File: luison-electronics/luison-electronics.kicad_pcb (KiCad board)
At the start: 2 copper layers, 83.2 x 64.8 mm, 26 parts, among them SW3 EECO_Micro-Dip_3500_B02, U2 Robochallenge_KillSwitch

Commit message: asd
asd
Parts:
- added PS10: COOLER, luison-electronics:JST_XH_B3B-XH-A_1x03_P2.50mm_Vertical, F.Cu at (175.9, 116.8)
- moved ? 3.18 mm to (167.6, 104.8)
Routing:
- net +24V: track 184.4 -> 191.5 mm
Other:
- board text added: "+24"
- board text added: "G"
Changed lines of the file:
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@@
   (net 41 "/6")
   (net 42 "/7")
+  (net 43 "unconnected-(PS10-Signal-Pad2)")
   (footprint "luison-electronics:JST_XH_B3B-XH-A_1x03_P2.50mm_Vertical" (layer "F.Cu")
     (at 182.245 108.585)
@@
   )
   (footprint "" (layer "F.Cu")
-    (at 170.815 104.775)
+    (at 167.64 104.775)
     (fp_text reference "" (at 0 0) (layer "F.SilkS")
         (effects (font (size 1.27 1.27) (thickness 0.15)))
@@
     (pad "1" thru_hole roundrect (at 0 0 90) (size 1.524 2.54) (drill 1) (layers "*.Cu" "*.Mask") (roundrect_rratio 0.25)
       (net 1 "GND"))
+  )
+  (footprint "luison-electronics:JST_XH_B3B-XH-A_1x03_P2.50mm_Vertical" (layer "F.Cu")
+    (at 175.895 116.84 180)
+    (descr "JST XH series connector, B3B-XH-A (http://www.jst-mfg.com/product/pdf/eng/eXH.pdf), generated with kicad-footprint-generator")
+    (tags "connector JST XH vertical")
+    (property "Sheetfile" "luison-electronics.kicad_sch")
+    (property "Sheetname" "")
+    (property "ki_description" "Omron Infrared Proximity Sensor")
+    (property "ki_keywords" "Digital Infrared Sensor")
+    (attr through_hole)
+    (fp_text reference "PS10" (at 2.5 -3.55) (layer "F.SilkS")
+        (effects (font (size 1 1) (thickness 0.15)))
+    )
+    (fp_text value "COOLER" (at 2.5 4.6) (layer "F.Fab")
+        (effects (font (size 1 1) (thickness 0.15)))
+    )
+    (fp_text user "${REFERENCE}" (at 2.5 2.7) (layer "F.Fab")
+        (effects (font (size 1 1) (thickness 0.15)))
+    )
+    (fp_line (start -2.85 -2.75) (end -2.85 -1.5)
+      (stroke (width 0.12) (type solid)) (layer "F.SilkS"))
+    (fp_line (start -2.56 -2.46) (end -2.56 3.51)
+      (stroke (width 0.12) (type solid)) (layer "F.SilkS"))
+    (fp_line (start -2.56 3.51) (end 7.56 3.51)
+      (stroke (width 0.12) (type solid)) (layer "F.SilkS"))
+    (fp_line (start -2.55 -2.45) (end -2.55 -1.7)
+      (stroke (width 0.12) (type solid)) (layer "F.SilkS"))
+    (fp_line (start -2.55 -1.7) (end -0.75 -1.7)
+      (stroke (width 0.12) (type solid)) (layer "F.SilkS"))
+    (fp_line (start -2.55 -0.2) (end -1.8 -0.2)
+      (stroke (width 0.12) (type solid)) (layer "F.SilkS"))
+    (fp_line (start -1.8 -0.2) (end -1.8 2.75)
+      (stroke (width 0.12) (type solid)) (layer "F.SilkS"))
+    (fp_line (start -1.8 2.75) (end 2.5 2.75)
+      (stroke (width 0.12) (type solid)) (layer "F.SilkS"))
+    (fp_line (start -1.6 -2.75) (end -2.85 -2.75)
+      (stroke (width 0.12) (type solid)) (layer "F.SilkS"))
+    (fp_line (start -0.75 -2.45) (end -2.55 -2.45)
+      (stroke (width 0.12) (type solid)) (layer "F.SilkS"))
+    (fp_line (start -0.75 -1.7) (end -0.75 -2.45)
+      (stroke (width 0.12) (type solid)) (layer "F.SilkS"))
+    (fp_line (start 0.75 -2.45) (end 0.75 -1.7)
+      (stroke (width 0.12) (type solid)) (layer "F.SilkS"))
+    (fp_line (start 0.75 -1.7) (end 4.25 -1.7)
+      (stroke (width 0.12) (type solid)) (layer "F.SilkS"))
+    (fp_line (start 4.25 -2.45) (end 0.75 -2.45)
+      (stroke (width 0.12) (type solid)) (layer "F.SilkS"))
+    (fp_line (start 4.25 -1.7) (end 4.25 -2.45)
+      (stroke (width 0.12) (type solid)) (layer "F.SilkS"))
+    (fp_line (start 5.75 -2.45) (end 5.75 -1.7)
+      (stroke (width 0.12) (type solid)) (layer "F.SilkS"))
+    (fp_line (start 5.75 -1.7) (end 7.55 -1.7)
+      (stroke (width 0.12) (type solid)) (layer "F.SilkS"))
+    (fp_line (start 6.8 -0.2) (end 6.8 2.75)
+      (stroke (width 0.12) (type solid)) (layer "F.SilkS"))
+    (fp_line (start 6.8 2.75) (end 2.5 2.75)
+      (stroke (width 0.12) (type solid)) (layer "F.SilkS"))
+    (fp_line (start 7.55 -2.45) (end 5.75 -2.45)
+      (stroke (width 0.12) (type solid)) (layer "F.SilkS"))
+    (fp_line (start 7.55 -1.7) (end 7.55 -2.45)
+      (stroke (width 0.12) (type solid)) (layer "F.SilkS"))
+    (fp_line (start 7.55 -0.2) (end 6.8 -0.2)
+      (stroke (width 0.12) (type solid)) (layer "F.SilkS"))
+    (fp_line (start 7.56 -2.46) (end -2.56 -2.46)
+      (stroke (width 0.12) (type solid)) (layer "F.SilkS"))
+    (fp_line (start 7.56 3.51) (end 7.56 -2.46)
+      (stroke (width 0.12) (type solid)) (layer "F.SilkS"))
+    (fp_line (start -2.95 -2.85) (end -2.95 3.9)
+      (stroke (width 0.05) (type solid)) (layer "F.CrtYd"))
+    (fp_line (start -2.95 3.9) (end 7.95 3.9)
+      (stroke (width 0.05) (type solid)) (layer "F.CrtYd"))
+    (fp_line (start 7.95 -2.85) (end -2.95 -2.85)
+      (stroke (width 0.05) (type solid)) (layer "F.CrtYd"))
+    (fp_line (start 7.95 3.9) (end 7.95 -2.85)
+      (stroke (width 0.05) (type solid)) (layer "F.CrtYd"))
+    (fp_line (start -2.45 -2.35) (end -2.45 3.4)
+      (stroke (width 0.1) (type solid)) (layer "F.Fab"))
+    (fp_line (start -2.45 3.4) (end 7.45 3.4)
+      (stroke (width 0.1) (type solid)) (layer "F.Fab"))
+    (fp_line (start -0.625 -2.35) (end 0 -1.35)
+      (stroke (width 0.1) (type solid)) (layer "F.Fab"))
+    (fp_line (start 0 -1.35) (end 0.625 -2.35)
+      (stroke (width 0.1) (type solid)) (layer "F.Fab"))
+    (fp_line (start 7.45 -2.35) (end -2.45 -2.35)
+      (stroke (width 0.1) (type solid)) (layer "F.Fab"))
+    (fp_line (start 7.45 3.4) (end 7.45 -2.35)
+      (stroke (width 0.1) (type solid)) (layer "F.Fab"))
+    (pad "1" thru_hole roundrect (at 0 0 180) (size 1.7 2.54) (drill 1) (layers "*.Cu" "*.Mask") (roundrect_rratio 0.147059)
+      (net 4 "+24V") (pinfunction "VCC") (pintype "power_in"))
+    (pad "2" thru_hole oval (at 2.5 0 180) (size 1.7 2.54) (drill 1) (layers "*.Cu" "*.Mask")
+      (net 43 "unconnected-(PS10-Signal-Pad2)") (pinfunction "Signal") (pintype "output"))
+    (pad "3" thru_hole oval (at 5 0 180) (size 1.7 2.54) (drill 1) (layers "*.Cu" "*.Mask")
+      (net 1 "GND") (pinfunction "GND") (pintype "power_in"))
+    (model "${KICAD6_3DMODEL_DIR}/Connector_JST.3dshapes/JST_XH_B3B-XH-A_1x03_P2.50mm_Vertical.wrl"
+      (offset (xyz 0 0 0))
+      (scale (xyz 1 1 1))
+      (rotate (xyz 0 0 0))
+    )
   )
   (footprint "luison-electronics:ESP32-S2-DevKitC-1" (layer "F.Cu")
@@
     (effects (font (size 1.5 1.5) (thickness 0.3) bold) (justify left bottom))
   )
+  (gr_text "G" (at 165.1 119.38) (layer "F.Cu" knockout)
+    (effects (font (size 1.5 1.5) (thickness 0.3) bold) (justify left bottom))
+  )
   (gr_text "PSFR\n" (at 181.61 115.57) (layer "F.Cu" knockout)
     (effects (font (size 1.5 1.5) (thickness 0.3) bold) (justify left bottom))
@@
     (effects (font (size 1.5 1.5) (thickness 0.3) bold) (justify left bottom))
   )
-  (gr_text "PSFC" (at 170.815 115.57) (layer "F.Cu" knockout)
+  (gr_text "PSFC" (at 171.45 106.045) (layer "F.Cu" knockout)
+    (effects (font (size 1.5 1.5) (thickness 0.3) bold) (justify left bottom))
+  )
+  (gr_text "+24" (at 179.705 119.38) (layer "F.Cu" knockout)
     (effects (font (size 1.5 1.5) (thickness 0.3) bold) (justify left bottom))
   )
@@
   (segment (start 125.08 104.7515) (end 125.08 108.585) (width 1.5) (layer "B.Cu") (net 2))
   (segment (start 125.08 110.475) (end 125.08 108.585) (width 1.5) (layer "B.Cu") (net 2))
+  (segment (start 175.895 116.84) (end 175.895 109.935) (width 1.25) (layer "B.Cu") (net 4))
   (segment (start 182.245 108.585) (end 182.245 112.649) (width 1.5) (layer "B.Cu") (net 4))
   (segment (start 186.715 66.065) (end 172.745 66.065) (width 1.5) (layer "B.Cu") (net 4))
@@
   (segment (start 190.119 111.633) (end 188.595 113.157) (width 1.5) (layer "B.Cu") (net 4))
   (segment (start 183.896 88.265) (end 187.706 92.075) (width 1.5) (layer "B.Cu") (net 4))
+  (segment (start 175.895 109.935) (end 175.815 109.855) (width 1.25) (layer "B.Cu") (net 4))
   (segment (start 172.745 66.065) (end 172.72 66.04) (width 1.5) (layer "B.Cu") (net 4))
   (segment (start 115.316 93.265) (end 172.5305 93.265) (width 1.5) (layer "B.Cu") (net 8))

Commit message: asdf
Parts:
- removed ? (x4): , 
- removed the REF** at (141.6, 113.0)
- moved REF** 0.76 mm to (190.5, 63.0)
- renumbered PS10 to COOLER
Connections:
- MCU2 pad 24: /LS_FR -> unconnected-(MCU2-IO43-Pad24)
- MCU2 pad 25: /SDA -> /LS_FR
- MCU2 pad 26: /SCL -> /LS_BR
- MCU2 pad 27: unconnected-(MCU2-IO2/ADC-Pad27) -> /SDA
- MCU2 pad 28: /LS_BR -> /SCL
- MCU2 pad 31: /SW_P8 -> unconnected-(MCU2-IO39-Pad31)
- MCU2 pad 32: unconnected-(MCU2-IO38-Pad32) -> /SW_P8
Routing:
- net /PS_R: track 23.5 -> 15.8 mm
- net /SDA: track 21.2 -> 28.4 mm
- net /SCL: track 25.0 -> 31.9 mm
- net /LS_BR: track 7.69 -> 11.3 mm
- net /LS_FR: track 8.22 -> 9.27 mm
- net /SW_P8: track 5.71 -> 6.73 mm
- net GND: vias 0 -> 6
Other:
- board size 83.2 x 64.8 mm -> 94 x 71.8 mm
- board text added: "LUISON_ELECTRONIS"
- board text removed: "++G5"
- board text removed: "+24"
- board text removed: "764"
- board text removed: "G"
- board text removed: "G EM S +"
- board text removed: "LSBL"
- board text removed: "LSBR"
- board text removed: "LSFL"
- board text removed: "LSFR"
- board text removed: "LUISON"
- board text removed: "PSB"
- board text removed: "PSFC"
- board text removed: "PSFL"
- board text removed: "PSFR"
- board text removed: "PSL"
- board text removed: "PSR"

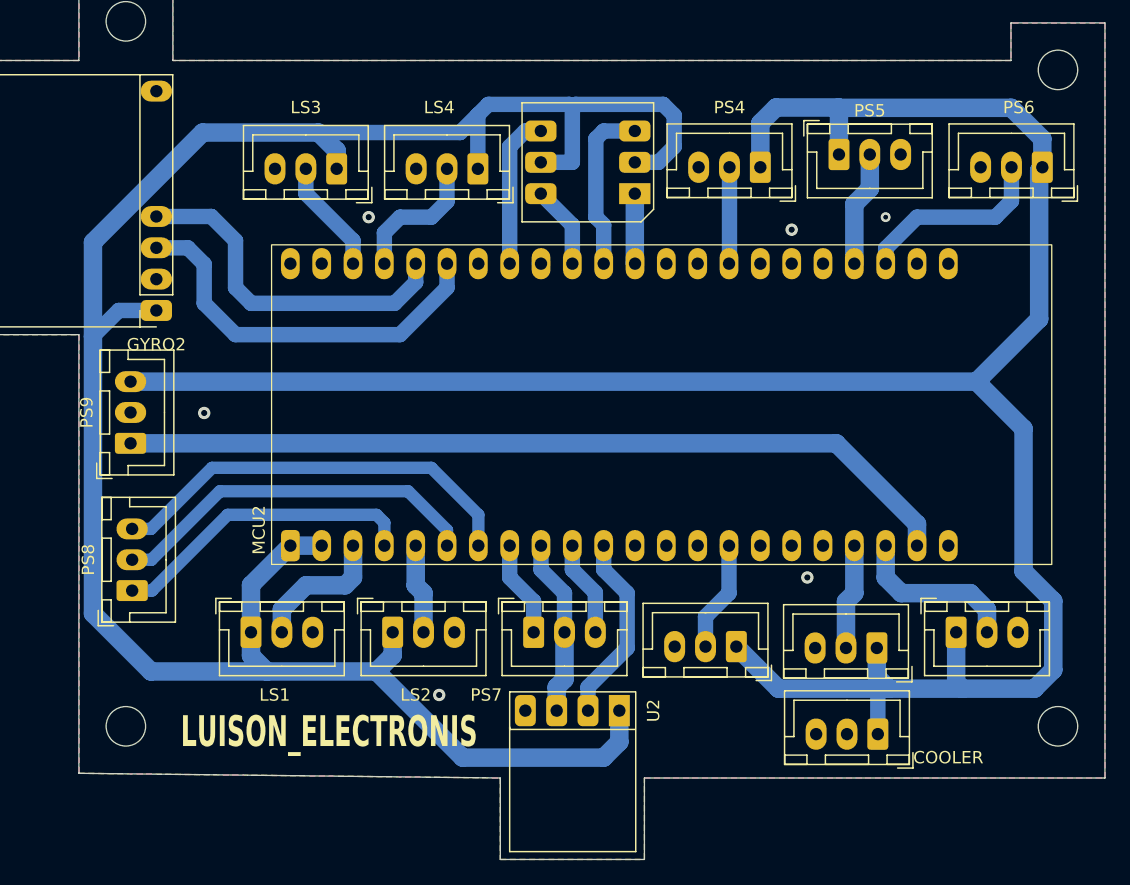
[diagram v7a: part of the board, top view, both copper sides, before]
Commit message: Update pcb with correct pins and constraints
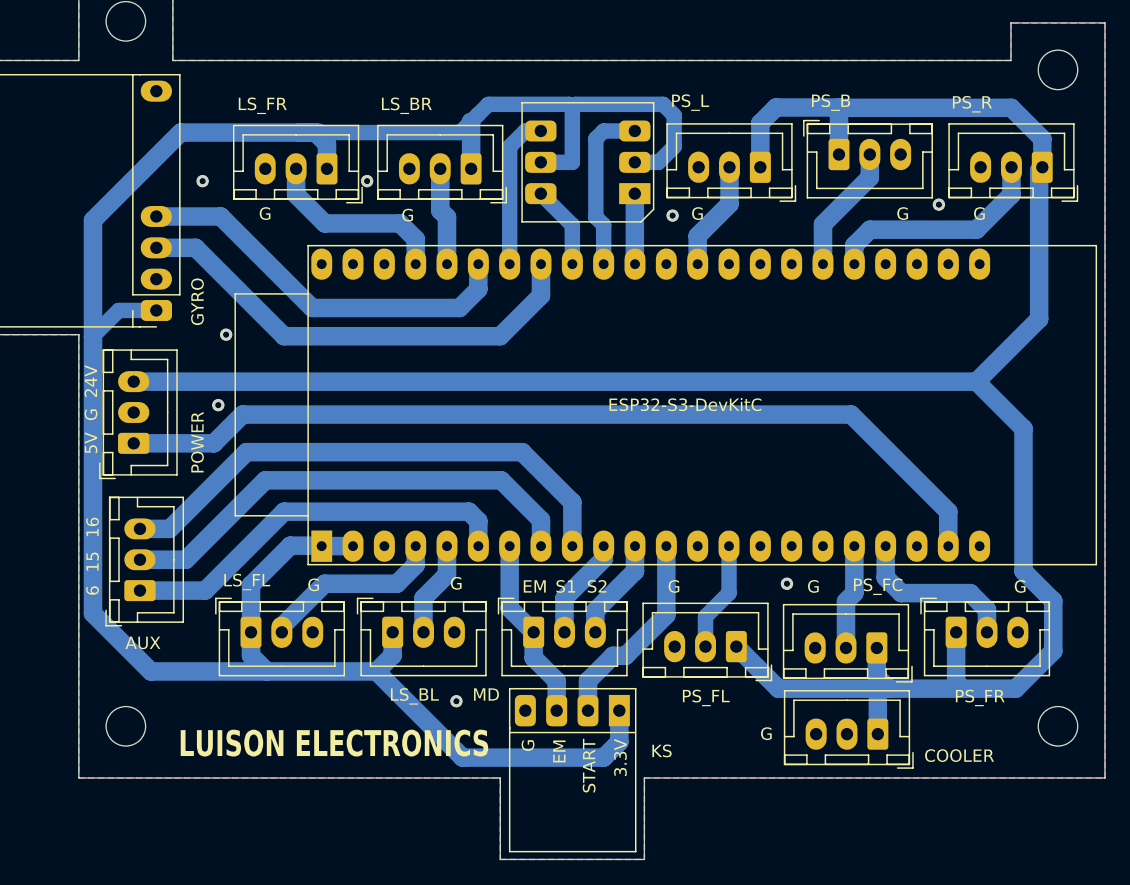
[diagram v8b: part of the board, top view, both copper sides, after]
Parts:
- removed MCU2: ESP32-S2-DevKitC-1, luison-electronics:ESP32-S2-DevKitC-1
- removed REF** (x4): MountingHole_3.2mm_M3, MountingHole:MountingHole_3.2mm_M3
- added H1: MountingHole, MountingHole:MountingHole_3.2mm_M3, F.Cu at (114.9, 59.1)
- added H2: MountingHole, MountingHole:MountingHole_3.2mm_M3, F.Cu at (190.5, 63.0)
- added H3: MountingHole, MountingHole:MountingHole_3.2mm_M3, F.Cu at (190.5, 116.2)
- added H4: MountingHole, MountingHole:MountingHole_3.2mm_M3, F.Cu at (114.9, 116.2)
- added U1: ESP32-S3-DevKitC, luison-electronics:ESP32-S3-DevKitC, F.Cu at (130.8, 101.6)
- AUX: renamed from PS8; value alimentacion_driver -> gpio_aux
- moved LS_FR 0.79 mm to (131.2, 71.0)
- moved AUX 0.64 mm to (116.1, 105.2)
- moved LS_BR 0.55 mm to (142.9, 71.0)
- moved POWER 0.25 mm to (115.6, 93.3)
- renumbered GYRO2 to GYRO, LS2 to LS_BL, LS4 to LS_BR, LS1 to LS_FL, LS3 to LS_FR, PS7 to MD, PS9 to POWER, PS5 to PS_B, PS2 to PS_FC, PS1 to PS_FL, PS3 to PS_FR, PS4 to PS_L, PS6 to PS_R
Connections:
- AUX pad 1: /4 -> /AUX6
- AUX pad 2: /6 -> /AUX15
- AUX pad 3: /7 -> /AUX16
- MD pad 1: /TX1_MD -> /KS_EM
- MD pad 2: /KS_EM -> /TX1_MD
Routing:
- net /AUX16: track 0.00 -> 42.9 mm
- net /AUX15: track 0.00 -> 38.6 mm
- net /7: track 34.2 -> 0.00 mm
- net /AUX6: track 0.00 -> 32.4 mm
- net /6: track 30.4 -> 0.00 mm
- net /4: track 25.1 -> 0.00 mm
- net /SCL: track 31.9 -> 38.1 mm
- net /LS_FR: track 9.27 -> 15.3 mm
- net +5V: track 68.2 -> 73.3 mm
- net +3.3V: track 178.5 -> 182.6 mm
- net +24V: track 191.5 -> 187.4 mm
- net /LS_FL: track 11.3 -> 14.9 mm
- net /SDA: track 28.4 -> 31.8 mm
- net /LS_BR: track 11.3 -> 7.96 mm
- net /PS_R: track 15.8 -> 18.2 mm
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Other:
- outline, holes or cut-outs redrawn
- board text added: "3.3V"
- board text added: "EM"
- board text added: "G"
- board text added: "KS"
- board text added: "LUISON ELECTRONICS"
- board text added: "S1"
- board text added: "S2"
- board text added: "START"
- board text removed: "LUISON_ELECTRONIS"
